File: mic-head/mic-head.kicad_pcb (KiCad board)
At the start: 2 copper layers, 22 x 40 mm, 16 parts, among them J1 Loetpads_Kabel_5x, U1 LP5907MFX-2.8, U2 OPA2325

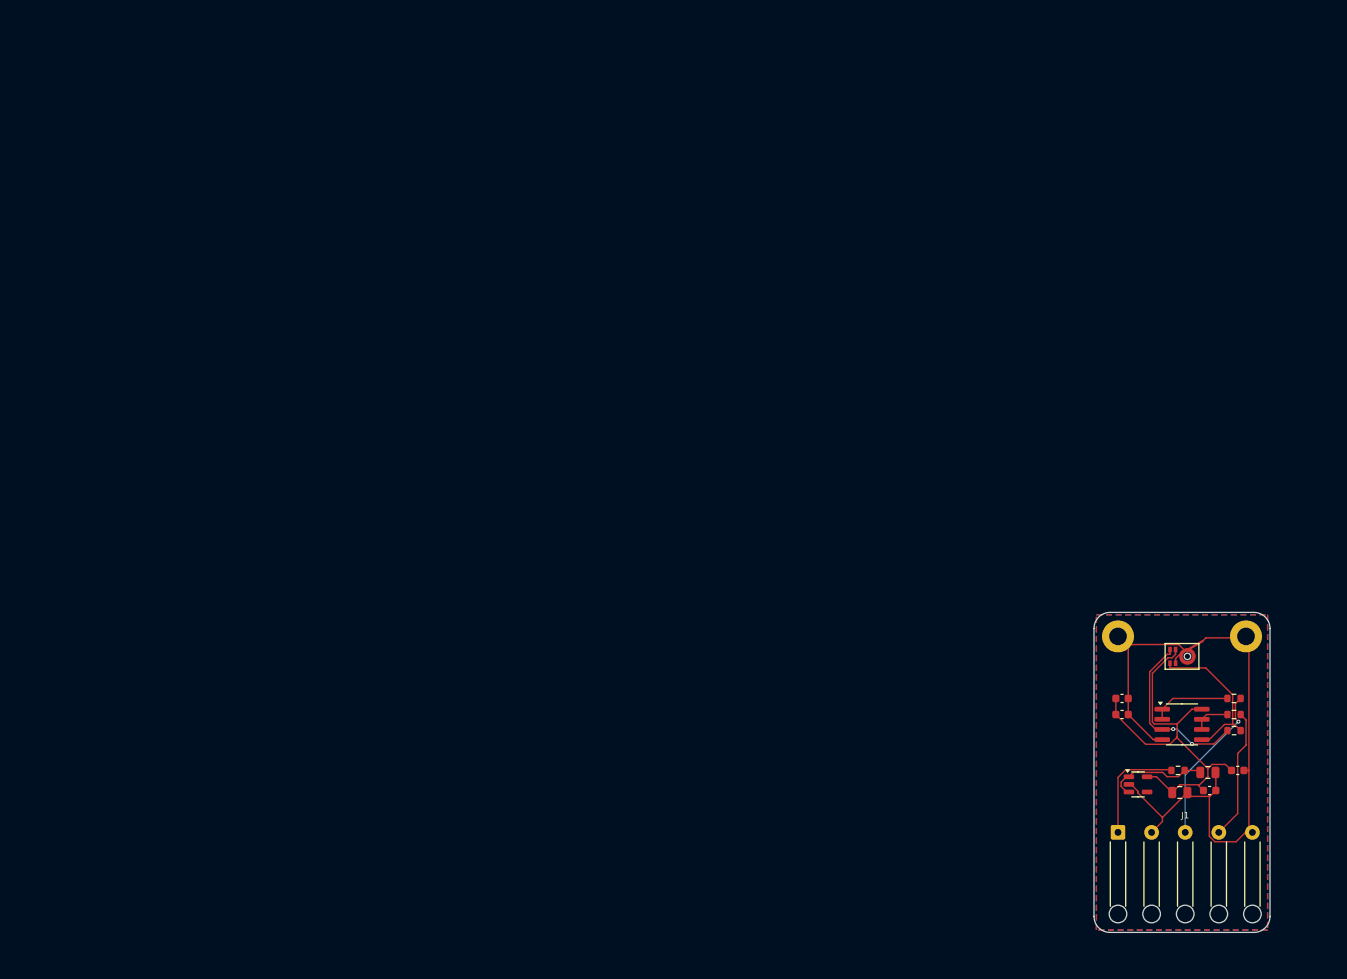
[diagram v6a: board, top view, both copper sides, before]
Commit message: Mikrofonkopf von 22 x 40 auf 8 x 27 mm
Kevin wollte den Kopf so schmal wie moeglich und hat dafuer Zugentlastung,
Befestigungsbohrungen, einseitige Bestueckung und den dickeren Draht
freigegeben. 880 mm2 auf 216 mm2 bei gleichen vierzehn Bauteilen.

Der groesste Posten war ein einziges Landmuster: die Loetpads mit
Zugentlastung massen 20,05 x 13,27 mm und damit 266 von 387 mm2
Bauteilflaeche - mehr als die anderen dreizehn Teile zusammen. Fuenf Pads
nebeneinander sind allein 20 mm breit und haben die Platinenbreite
diktiert. Ersatz ist lib/exhaust-mic.pretty/
SolderWire-0.1sqmm_1x05_2reihig_P2.6mm: zwei versetzte Spalten auf
5,15 x 7,35 mm, die Draehte laufen laengs aus der Platine statt quer.

Zwei Stolpersteine:
- Die Durchsteckpads sperren die Rueckseite auf ihrer ganzen Flaeche.
  C1, C4 und FB1 sitzen deshalb vorn zwischen Wandler und Kabelpads.
- Bei 8 mm Breite muss links ein 2,7 mm breiter Kanal frei bleiben. Erst
  blieb OUT_P als einziges Netz offen, weil U1 im Weg stand; OUT_N kam
  rechts durch. Ab y 9,9 ist auf der Rueckseite alles nach rechts gerueckt.

Dabei gefunden: freerouting haelt zur Begrenzung nur den allgemeinen
Abstand ein (0,15 mm), KiCad verlangt zur Platinenkante 0,25 mm. Auf dem
schmalen Kopf lagen drei Bahnen mit 0,23 mm an der Kante - drei
Regelfehler. route.kontur_einruecken() verkleinert die Begrenzung im DSN
jetzt um 0,12 mm, gerechnet auf den DSN-Koordinaten selbst.

Ergebnis Mikrofonkopf: 0 offene Verbindungen, 0 DRC-Fehler, 0 DRC-
Warnungen, 0 ERC-Fehler, 0 Schaltplanparitaet. Bauhoehe 1,8 mm oben,
1,5 mm unten - mit 1,6 mm Platine rund 4,9 mm Gesamtaufbau.

Das Roehrchen muss jetzt klemmen oder vergiessen und den Kabelzug
abfangen; beides stand vorher auf der Platine.
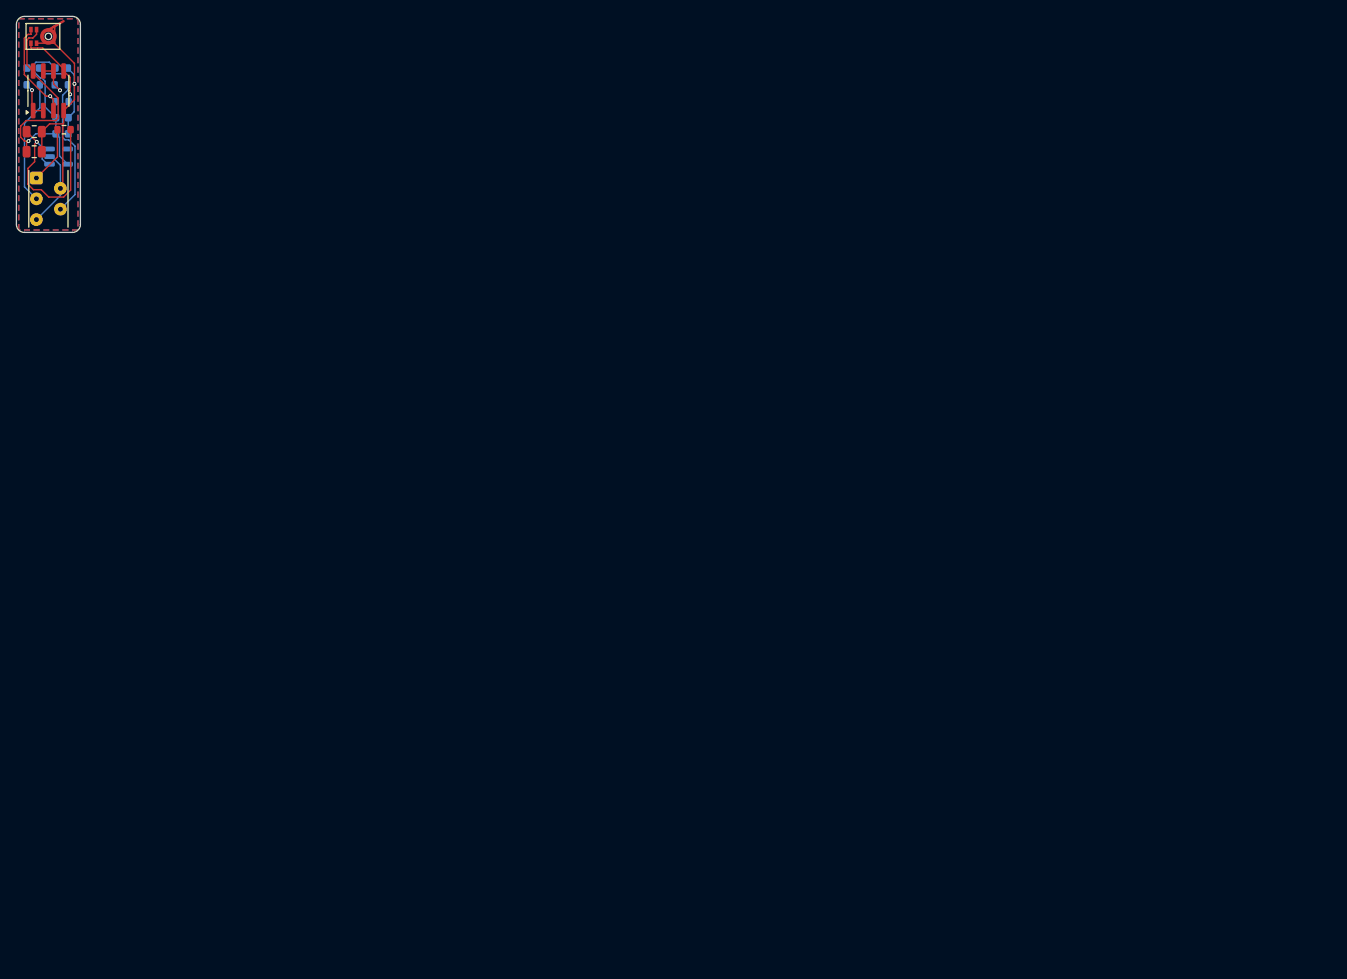
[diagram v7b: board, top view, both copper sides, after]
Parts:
- removed H1, H2: , 
- C3, C5, C6, C7, R1, R2, R3, U1: moved to B.Cu
- J1: footprint Connector_Wire:SolderWire-0.25sqmm_1x05_P4.2mm_D0.65mm_OD1.7mm_Relief -> exhaust-mic:SolderWire-0.1sqmm_1x05_2reihig_P2.6mm
- moved R1 168.6 mm to (2.10, 8.55)
- moved C3 168.1 mm to (5.71, 12.7)
- moved C1 167.2 mm to (2.23, 14.4)
- moved R2 166.4 mm to (5.61, 8.55)
- moved R3 166.3 mm to (5.71, 10.7)
- moved C7 165.3 mm to (5.71, 14.7)
- moved C4 164.1 mm to (2.23, 16.9)
- moved U2 162.3 mm to (4.00, 9.30), turned to 90 degrees
- moved MK1 162.1 mm to (3.32, 2.50)
- moved FB1 160.6 mm to (5.96, 14.2)
- moved C5 157.3 mm to (2.10, 6.46)
- moved U1 156.1 mm to (5.28, 17.5)
- moved J1 155.4 mm to (4.00, 22.8)
- moved C6 155.3 mm to (5.61, 6.46)
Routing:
- net SHIELD: track 89.0 -> 54.8 mm, vias 0 -> 1
- net Net-(U1-EN): track 12.8 -> 26.0 mm, vias 0 -> 1
- net /MIC_N: track 19.5 -> 10.3 mm, vias 0 -> 1
- net /MIC_P: track 22.0 -> 13.4 mm, vias 2 -> 1
- net VIN_3V3: track 14.0 -> 7.13 mm
- net +2V8: track 50.9 -> 44.6 mm, vias 0 -> 1
- net /BUF_P: track 9.98 -> 4.83 mm, vias 0 -> 1
- net OUT_P: track 19.9 -> 15.7 mm, vias 1 -> 0
- net OUT_N: track 16.4 -> 17.5 mm
- net /BUF_N: track 4.72 -> 4.96 mm, vias 0 -> 1
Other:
- board size 22 x 40 mm -> 8 x 27 mm
- board text removed: "exhaust-mic Kopf"
